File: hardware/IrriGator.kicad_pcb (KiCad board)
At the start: 2 copper layers, 141.4 x 116.8 mm, 45 parts, among them J1 230VAC, J2 24VAC L, J3 24VAC N, J4 24VAC, J5 Conn_01x04_Socket, J6 Conn_01x04_Pin, J7 Conn_01x04_Pin, SW1 SW_Push, T1 24V 16VA, U1 LF33_TO220, U2 ESP-01v090, U3 DS3231-MINI-RTC, U4 ATtiny45-20P, U5 ATtiny45-20P

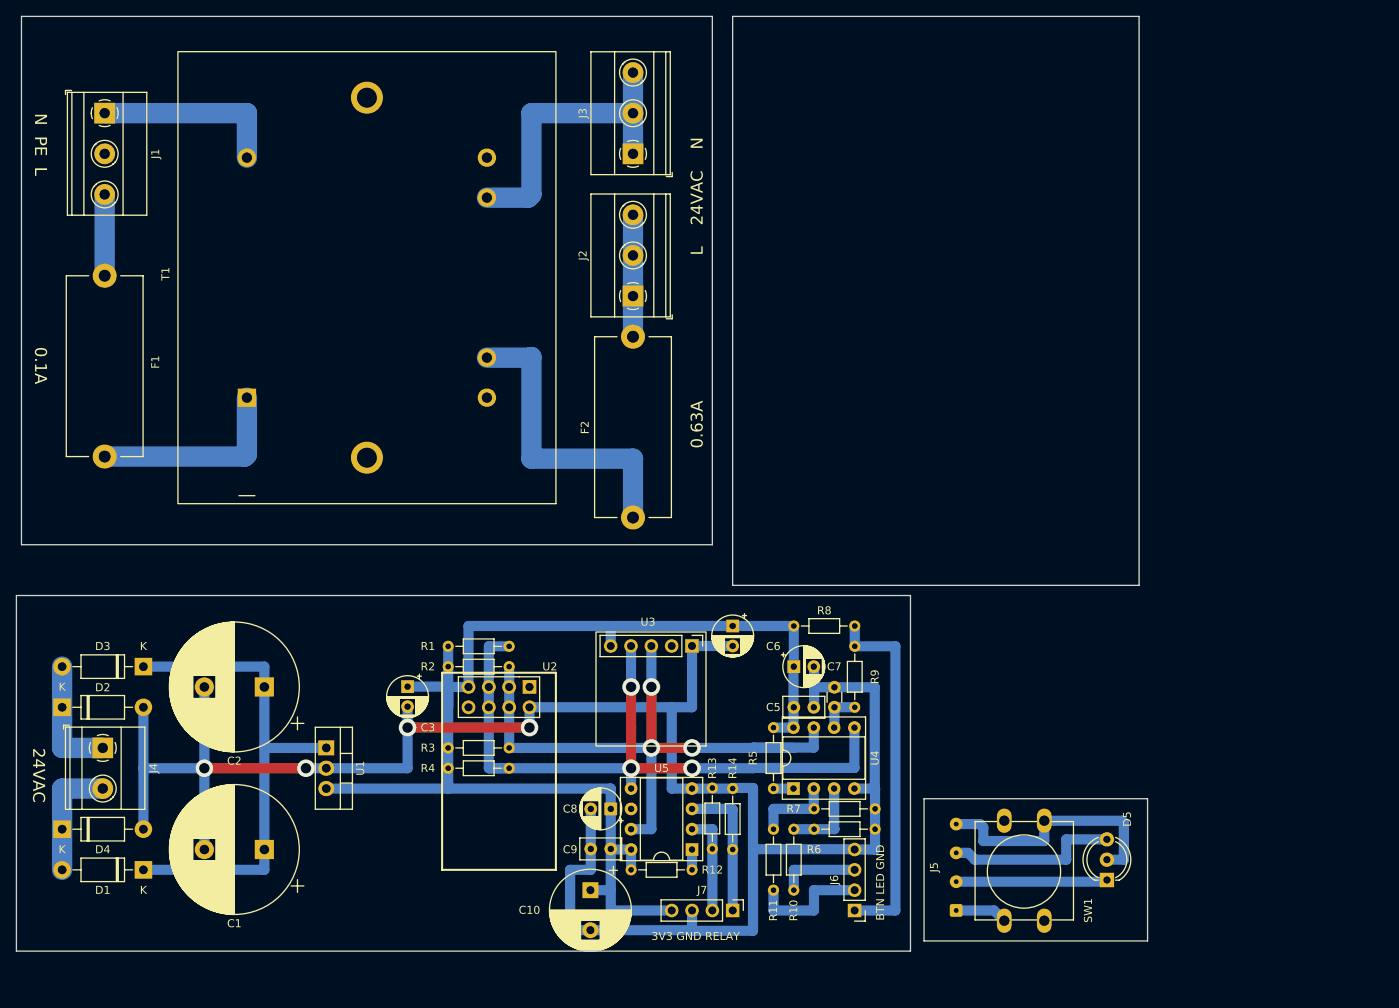
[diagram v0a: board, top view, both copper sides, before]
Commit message: Moved rectifier part to the transformer module, DC-DC stepdown becomes an external module
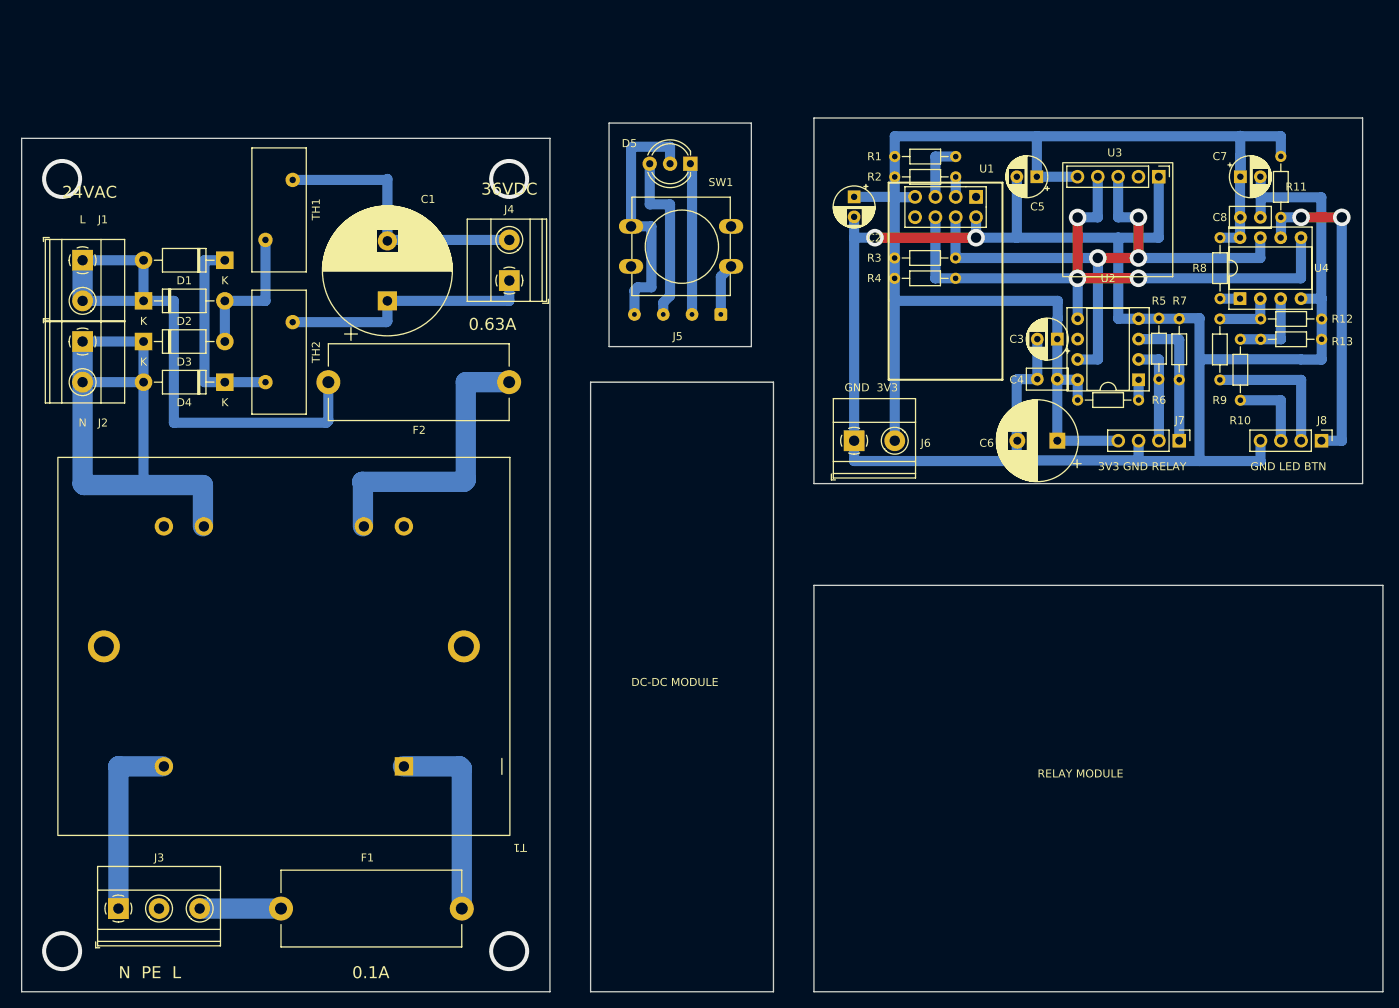
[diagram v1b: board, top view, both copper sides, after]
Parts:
- removed the C2 at (50.7, 104.1)
- removed the C7 at (121.9, 106.7)
- removed the R9 at (124.5, 106.7)
- removed the U1 at (58.4, 111.8)
- added J6: 3V3, TerminalBlock_Phoenix:TerminalBlock_Phoenix_MKDS-1,5-2-5.08_1x02_P5.08mm_Horizontal, F.Cu at (124.4, 73.4)
- added TH1: 33R 2.5A, Varistor:RV_Disc_D15.5mm_W6.8mm_P7.5mm, F.Cu at (50.8, 48.3)
- added TH2: 33R 2.5A, Varistor:RV_Disc_D15.5mm_W6.8mm_P7.5mm, F.Cu at (50.8, 66.0)
- C1: value 2200u -> 1000u
- C6: renamed from C10; value 470u -> 1000u
- J1: renamed from J2; value 24VAC L -> L; footprint TerminalBlock_Phoenix:TerminalBlock_Phoenix_MKDS-1,5-3-5.08_1x03_P5.08mm_Horizontal -> TerminalBlock_Phoenix:TerminalBlock_Phoenix_MKDS-1,5-2-5.08_1x02_P5.08mm_Horizontal
- J2: renamed from J3; value 24VAC N -> N; footprint TerminalBlock_Phoenix:TerminalBlock_Phoenix_MKDS-1,5-3-5.08_1x03_P5.08mm_Horizontal -> TerminalBlock_Phoenix:TerminalBlock_Phoenix_MKDS-1,5-2-5.08_1x02_P5.08mm_Horizontal
- J4: value 24VAC -> 36VDC
- R10: value 10 -> 47
- moved D5 103.6 mm to (103.9, 38.7), turned to 180 degrees
- moved J3 99.4 mm to (32.4, 131.8), turned to 0 degrees
- moved SW1 90.5 mm to (96.5, 46.6), turned to 0 degrees
- moved R9 84.7 mm to (170.1, 58.1)
- moved R11 84.6 mm to (177.7, 37.8), turned to -90 degrees
- moved U1 82.9 mm to (139.6, 42.9)
- moved C8 82.9 mm to (175.2, 45.4)
- moved R10 82.9 mm to (172.7, 60.7)
- moved C7 82.9 mm to (172.7, 40.4)
- moved R12 82.9 mm to (175.2, 58.1)
- moved R13 82.9 mm to (175.2, 60.7)
- moved R8 82.9 mm to (170.1, 48.0)
- moved U4 82.9 mm to (172.6, 55.6)
- moved R3 82.8 mm to (129.5, 50.5)
- moved R4 82.8 mm to (129.5, 53.1)
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- renumbered C3 to C2, C8 to C3, C9 to C4, C4 to C5, C6 to C7, C5 to C8, J1 to J3, J6 to J8, R8 to R11, R7 to R12, R6 to R13, R13 to R5, R12 to R6, R14 to R7, R5 to R8, R11 to R9, U2 to U1, U5 to U2
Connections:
- D1 pad 1: +36V -> Net-(D1-K)
- D2 pad 1: Net-(D2-K) -> Net-(D1-A)
- D2 pad 2: GND -> Net-(D2-A)
- D3 pad 1: +36V -> Net-(D2-K)
- D3 pad 2: Net-(D2-K) -> Net-(D2-A)
- D4 pad 1: Net-(D1-A) -> Net-(D1-K)
- D4 pad 2: GND -> Net-(D2-K)
- F2 pad 2: Net-(J2-Pin_1) -> Net-(D1-A)
- J1 pad 1: Net-(J2-Pin_1) -> Net-(D1-A)
- J1 pad 2: Net-(J2-Pin_1) -> Net-(D1-A)
- J2 pad 1: Net-(J3-Pin_1) -> Net-(D2-K)
- J2 pad 2: Net-(J3-Pin_1) -> Net-(D2-K)
- J4 pad 1: Net-(D2-K) -> +36V
- J4 pad 2: Net-(D1-A) -> GND
- T1 pad 9: Net-(J3-Pin_1) -> Net-(D2-K)
- U4 pad 6: Net-(U4-PB1) -> Net-(J6-Pin_1)
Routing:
- net Net-(D2-K): track 15.2 -> 70.8 mm
- net Net-(D1-A): track 15.2 -> 68.7 mm
- net Net-(J3-Pin_1): track 38.7 -> 0.00 mm
- net +36V: track 63.4 -> 32.2 mm
- net Net-(D1-K): track 0.00 -> 25.4 mm
- net GND: track 259.1 -> 283.7 mm, vias 4 -> 2
- net Net-(D2-A): track 0.00 -> 17.8 mm
- net Net-(J2-Pin_1): track 15.2 -> 0.00 mm
- net VCC: track 159.9 -> 174.8 mm
- net Net-(J6-Pin_1): track 45.7 -> 40.6 mm, vias 0 -> 2
- net Net-(U4-PB1): track 5.10 -> 0.00 mm
- net SCL: track 76.3 -> 73.6 mm
- net Net-(U4-XTAL1/PB3): track 10.2 -> 7.58 mm
- net Net-(U2-RST): track 10.2 -> 7.62 mm
- net Net-(U2-CH_PD): track 5.08 -> 2.54 mm
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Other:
- board size 141.4 x 116.8 mm -> 170.2 x 109.2 mm
- board text added: "DC-DC MODULE"
- board text added: "GND 3V3"
- board text added: "GND LED BTN"
- board text added: "RELAY MODULE"
- board text removed: "BTN LED GND"
- board text removed: "L 24VAC N"

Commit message: Updated PCB layout to better match the actual build
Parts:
- C6: footprint Capacitor_THT:CP_Radial_D10.0mm_P5.00mm -> Capacitor_THT:CP_Radial_D8.0mm_P5.00mm
- R6, R8: value 30k -> 10k
- moved TH1 19.0 mm to (50.8, 67.2)
- moved TH2 15.2 mm to (50.8, 50.8)
- moved C1 7.62 mm to (66.0, 48.3), turned to -90 degrees
- moved C6 2.24 mm to (149.8, 71.1), turned to -90 degrees
- turned C5 to -90 degrees
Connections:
- D2 pad 1: Net-(D1-A) -> Net-(D2-K)
- D3 pad 1: Net-(D2-K) -> Net-(D1-A)
- J4 pad 1: +36V -> GND
- J4 pad 2: GND -> +36V
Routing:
- net GND: track 283.7 -> 277.6 mm, vias 2 -> 6
- net Net-(D2-A): track 17.8 -> 14.9 mm
- net SCL: track 73.6 -> 73.7 mm, vias 3 -> 4
- net Net-(J8-Pin_1): vias 2 -> 0

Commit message: Added UART debug pins to the hardware
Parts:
- added J8: Conn_01x02_Socket, Connector_PinSocket_2.54mm:PinSocket_1x02_P2.54mm_Vertical, F.Cu at (142.3, 40.6)
- C6: footprint Capacitor_THT:CP_Radial_D8.0mm_P5.00mm -> Capacitor_THT:CP_Radial_D10.0mm_P5.00mm
- moved J6 2.82 mm to (182.9, 76.2)
- moved J7 2.82 mm to (165.1, 76.2)
- moved J5 2.82 mm to (124.5, 76.2)
- moved R12 2.82 mm to (175.3, 61.0)
- moved R13 2.82 mm to (175.3, 63.5)
- moved R2 2.82 mm to (129.6, 43.2)
- moved U1 2.82 mm to (139.7, 45.7)
- moved U3 2.82 mm to (162.6, 43.2)
- moved U4 2.82 mm to (172.7, 58.4)
- moved C2 2.82 mm to (124.5, 45.7)
- moved C5 2.82 mm to (147.3, 43.2)
- moved C7 2.82 mm to (172.8, 43.2)
- moved R10 2.82 mm to (172.8, 63.5)
- moved R11 2.82 mm to (177.8, 40.6)
- moved R3 2.82 mm to (129.5, 53.3)
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- renumbered J6 to J5, J8 to J6, J5 to J9
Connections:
- net Net-(J7-Pin_1) renamed /RELAY2
- net Net-(J7-Pin_2) renamed /RELAY1
- net Net-(J8-Pin_1) renamed /BTN
- net Net-(J8-Pin_2) renamed /RED
- net Net-(J8-Pin_3) renamed /BLUE
- U1 pad 1: unconnected-(U1-UTXD-Pad1) -> /TX
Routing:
- net GND: track 277.6 -> 287.7 mm
- net /TX: track 0.00 -> 4.80 mm
- net (no net): vias 4 -> 14
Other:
- board size 170.2 x 109.2 mm -> 170.2 x 108.6 mm
